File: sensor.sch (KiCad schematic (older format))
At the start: 53 parts, among them CON1 USB_B_Micro, U1 ESP-12F, U2 HTU21D, U3 PMS7003

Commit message: Use libraries from KiCad 4.0.7 instead of new from KiCad GitHub.
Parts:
- removed CON1: USB_B_Micro, Connectors_USB:USB_Micro-B_Molex-105017-0001, symbol USB_B_Micro
- added C?: 10uF/10V, Capacitor_SMD:C_0805_2012Metric, symbol C
- added C?: 100nF, Capacitor_SMD:C_0603_1608Metric, symbol C
- added CON1: Micro USB, Connectors_USB:USB_Micro-B_Molex-105017-0001, symbol USB_OTG
- added R? (x4): 10k, symbol R
- R13, R14, R15, R16: value 4k7 -> 10k
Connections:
- wire segments 153 -> 141
- no-connect marks 0 -> 8

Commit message: Working on connections
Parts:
- removed R25, R28, R33, R6: 130, symbol R
- removed R4: 180, symbol R
- added C?: 100nF, Capacitors_SMD:C_0603, symbol C
- added J?: Conn_01x05, symbol Conn_01x05
- added R35: 180, Resistors_SMD:R_0603, symbol R
- added R36, R37, R38, R39: 130, Resistors_SMD:R_0603, symbol R
- added R?: 10k, Resistors_SMD:R_0603, symbol R
- added SW?: RESET, symbol SW_Push
- added SW?: CFG, symbol SW_Push
- added TP1: PMS_SET, Wire_Pads:SolderWirePad_single_0-8mmDrill, symbol TEST_1P
- added TP2: PMS_RESET, Wire_Pads:SolderWirePad_single_0-8mmDrill, symbol TEST_1P
- added TP?: CFG, Wire_Pads:SolderWirePad_single_0-8mmDrill, symbol TEST_1P
- added TP?: RESET, Wire_Pads:SolderWirePad_single_0-8mmDrill, symbol TEST_1P
- C1: footprint Capacitor_SMD:C_0603_1608Metric -> Capacitors_SMD:C_0603
- C2: footprint Capacitor_SMD:C_0805_2012Metric -> Capacitors_SMD:C_0805
- C3: renamed from C?; footprint Capacitor_SMD:C_0805_2012Metric -> Capacitors_SMD:C_0805
- C4: renamed from C?; footprint Capacitor_SMD:C_0603_1608Metric -> Capacitors_SMD:C_0603
- Q1, Q2, Q3: renamed from Q?; footprint (none) -> TO_SOT_Packages_SMD:SOT-23
- R1, R10, R11, R12, R13, R14, R15, R16, R18, R2, R20, R21, R22, R24, R26, R3, R31, R32, R8: footprint (none) -> Resistors_SMD:R_0603
- R17, R23, R29, R30, R7: value 180 -> 130; footprint (none) -> Resistors_SMD:R_0603
- R19, R27, R34, R5, R9: value 130 -> 180; footprint (none) -> Resistors_SMD:R_0603
- R25, R28, R4, R6: renamed from R?; footprint (none) -> Resistors_SMD:R_0603
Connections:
- net +5V: now also J?.5 (Pin_5)
- net GND: now also C?.2, J?.4 (Pin_4), R?.2, SW?.2, SW?.2
- net LED_B: now also R17.2, R18.2, R23.2, R24.2, R31.2, R32.2, R8.2, R38.2, R39.2; no longer R12.2, R19.2, R22.2, R34.2, R9.2
- net LED_G: now also R12.2, R22.2, R29.2, R30.2, R7.2, R36.2, R37.2; no longer R18.2, R24.2, R27.2, R31.2, R32.2, R5.2, R8.2
- net LED_R: now also R19.2, R27.2, R34.2, R5.2, R9.2, R35.2; no longer R17.2, R23.2, R29.2, R30.2, R7.2
- net PMS_RESET: now also TP2.1
- net RESET: now reaches R6.2, U1.1 (RST)
- net RESET: now also C?.1, SW?.1, TP?.1
- net at U1.16 (GPIO15/BOOT2): now also R?.1
- net CFG_BTN: now reaches R28.2, U1.18 (GPIO0/BOOT0)
- net CFG_BTN: now also SW?.1, TP?.1
- net ESP_RXD: now reaches U1.21 (GPIO3/UART0_RXD)
- net ESP_RXD: now also J?.3 (Pin_3)
- net ESP_TXD: now reaches U1.22 (GPIO1/UART0_TXD)
- net ESP_TXD: now also J?.2 (Pin_2)
- net PMS_SET: now reaches R13.2, U3.10 (SET)
- net PMS_SET: now also TP1.1
- net at D2.4 (RK): now also R9.1
- net at D2.3 (GK): now also R11.1; no longer R5.1
- net at D2.2 (BK): now also R17.1
- net at D3.4 (RK): now also R19.1; no longer R7.1
- net at D3.3 (GK): now also R21.1; no longer R8.1
- net at D3.2 (BK): now also R23.1; no longer R9.1
- net at D7.4 (RK): now also R26.1; no longer R10.1
- net at D7.3 (GK): now also R29.1; no longer R11.1
- net at D7.2 (BK): now also R31.1; no longer R12.1
- net at D9.4 (RK): now also R34.1; no longer R29.1
- net at D9.3 (GK): now also R36.1; no longer R31.1
- net at D9.2 (BK): now also R38.1
- net at D4.2 (BK): now also R8.1; no longer R19.1
- net at D4.3 (GK): now also R7.1; no longer R18.1
- net at D4.4 (RK): now also R5.1; no longer R17.1
- net at D5.4 (RK): now also R10.1; no longer R20.1
- net at D5.3 (GK): now also R12.1; no longer R21.1
- net at D5.2 (BK): now also R18.1; no longer R22.1
- net at D6.4 (RK): now also R20.1; no longer R23.1
- net at R24.1: now also D6.2 (BK); no longer D6.3 (GK)
- net at D8.4 (RK): now also R27.1; no longer R26.1
- net at D8.3 (GK): now also R30.1; no longer R27.1
- net at D8.2 (BK): now also R32.1
- net at D10.4 (RK): now also R35.1; no longer R30.1
- net at D10.3 (GK): now also R37.1; no longer R32.1
- net at D10.2 (BK): now also R39.1; no longer R34.1
- net MCU_RXD renamed PMS_TXD
- net MCU_TXD renamed PMS_RXD
- net SCL renamed HTU_SCL
- net SDA renamed HTU_SDA
- new net: D6.3 (GK), R22.1
- no-connect marks 8 -> 9
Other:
- moved on the sheet: C1, C2, C3, C4, D1, D10, D2, D3, D4, D5, D6, D7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

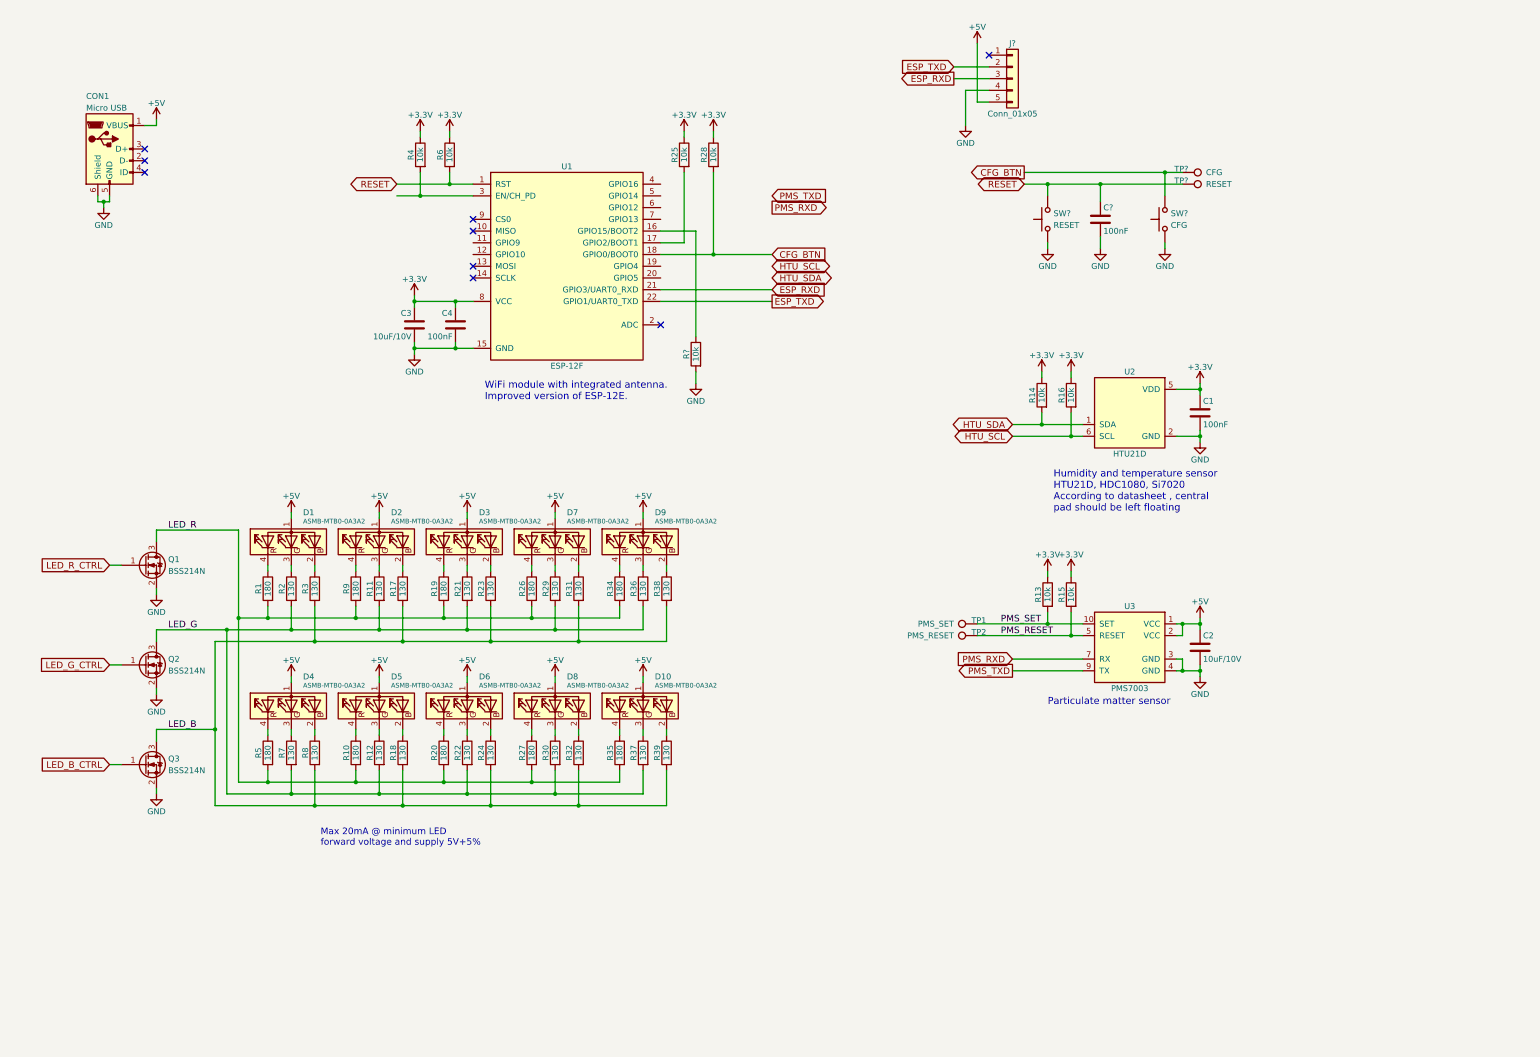
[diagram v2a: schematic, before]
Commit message: Add power supplies and other connections.
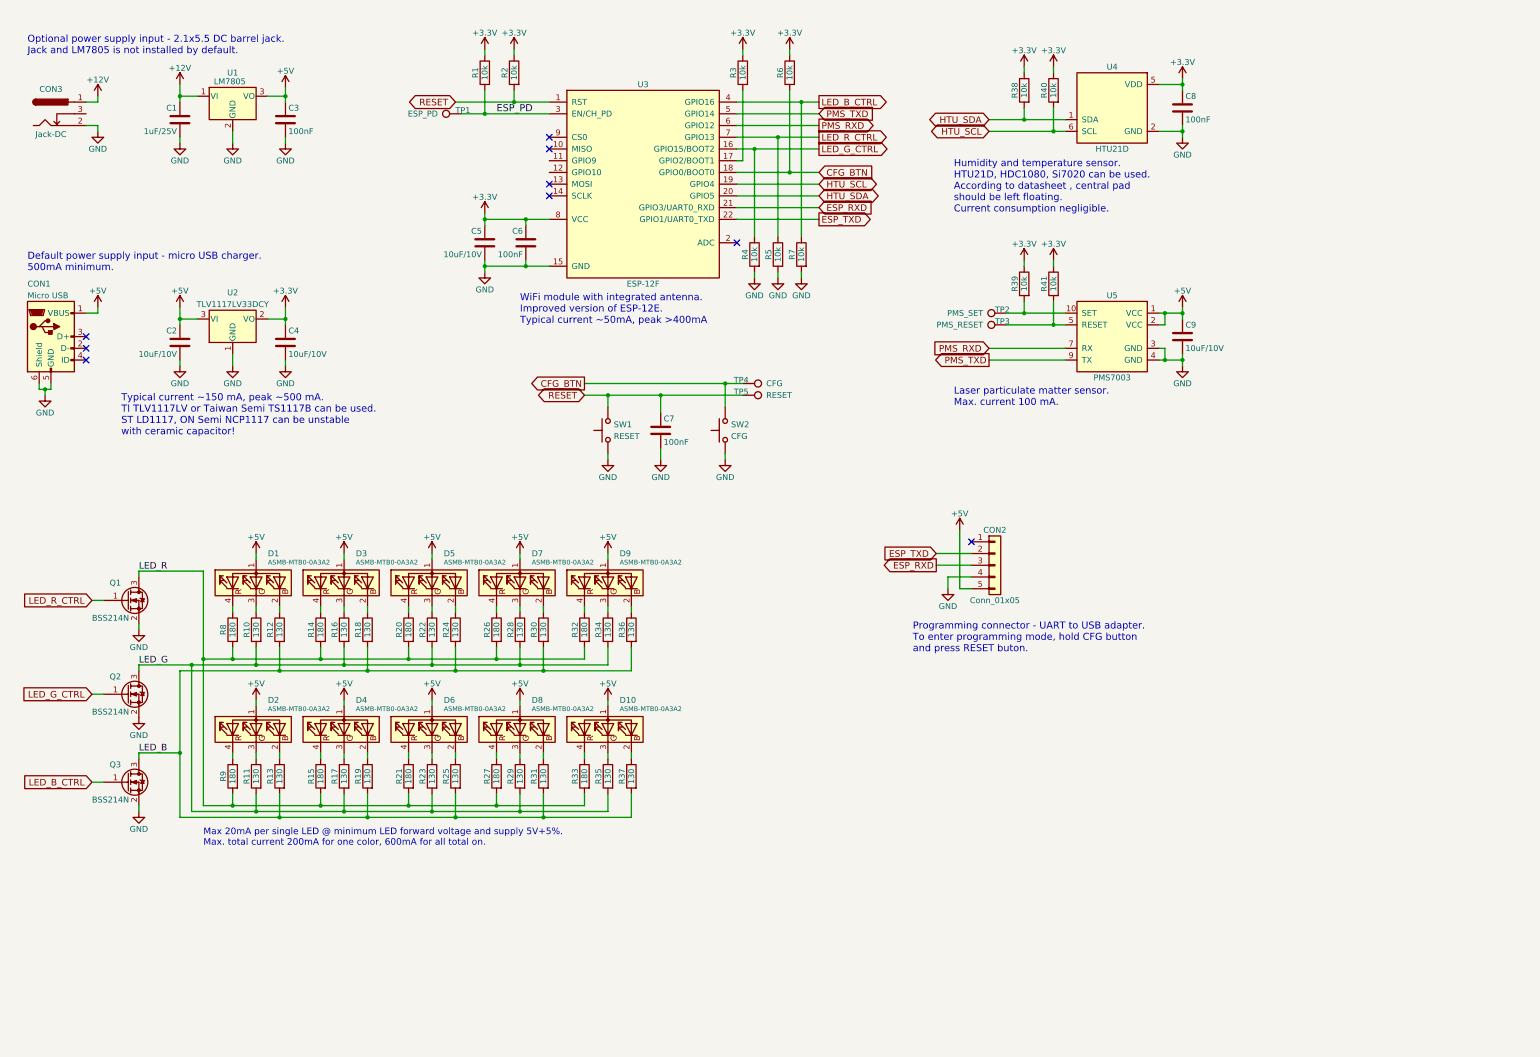
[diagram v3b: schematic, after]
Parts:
- added C1: 1uF/25V, Capacitors_SMD:C_0805, symbol C
- added C2, C4: 10uF/10V, Capacitors_SMD:C_0805, symbol C
- added C3: 100nF, Capacitors_SMD:C_0805, symbol C
- added CON3: Jack-DC, symbol Jack-DC
- added R5, R7: 10k, Resistors_SMD:R_1206, symbol R
- added TP1: ESP_PD, Wire_Pads:SolderWirePad_single_0-8mmDrill, symbol TEST_1P
- added U1: LM7805, TO_SOT_Packages_THT:TO-220_Horizontal, symbol LM7805_TO220
- added U2: TLV1117LV33DCY, TO_SOT_Packages_SMD:SOT-223-3Lead_TabPin2, symbol TLV1117-33
- C6: renamed from C4; footprint Capacitors_SMD:C_0603 -> Capacitors_SMD:C_0805
- C7: renamed from C?; footprint Capacitors_SMD:C_0603 -> Capacitors_SMD:C_0805
- C8: renamed from C1; footprint Capacitors_SMD:C_0603 -> Capacitors_SMD:C_0805
- CON2: renamed from J?; footprint (none) -> Pin_Headers:Pin_Header_Angled_1x05_Pitch2.54mm
- R1: renamed from R4; footprint Resistors_SMD:R_0603 -> Resistors_SMD:R_1206
- R10: renamed from R2; footprint Resistors_SMD:R_0603 -> Resistors_SMD:R_1206
- R11: renamed from R7; footprint Resistors_SMD:R_0603 -> Resistors_SMD:R_1206
- R12: renamed from R3; footprint Resistors_SMD:R_0603 -> Resistors_SMD:R_1206
- R13: renamed from R8; footprint Resistors_SMD:R_0603 -> Resistors_SMD:R_1206
- R14: renamed from R9; footprint Resistors_SMD:R_0603 -> Resistors_SMD:R_1206
- R15: renamed from R10; footprint Resistors_SMD:R_0603 -> Resistors_SMD:R_1206
- R16: renamed from R11; footprint Resistors_SMD:R_0603 -> Resistors_SMD:R_1206
- R17: renamed from R12; footprint Resistors_SMD:R_0603 -> Resistors_SMD:R_1206
- R18: renamed from R17; footprint Resistors_SMD:R_0603 -> Resistors_SMD:R_1206
- R19: renamed from R18; footprint Resistors_SMD:R_0603 -> Resistors_SMD:R_1206
- R2: renamed from R6; footprint Resistors_SMD:R_0603 -> Resistors_SMD:R_1206
- R20: renamed from R19; footprint Resistors_SMD:R_0603 -> Resistors_SMD:R_1206
- R21: renamed from R20; footprint Resistors_SMD:R_0603 -> Resistors_SMD:R_1206
- R22: renamed from R21; footprint Resistors_SMD:R_0603 -> Resistors_SMD:R_1206
- R23: renamed from R22; footprint Resistors_SMD:R_0603 -> Resistors_SMD:R_1206
- R24: renamed from R23; footprint Resistors_SMD:R_0603 -> Resistors_SMD:R_1206
- R25: renamed from R24; footprint Resistors_SMD:R_0603 -> Resistors_SMD:R_1206
- R26, R27: footprint Resistors_SMD:R_0603 -> Resistors_SMD:R_1206
- R28: renamed from R29; footprint Resistors_SMD:R_0603 -> Resistors_SMD:R_1206
- R29: renamed from R30; footprint Resistors_SMD:R_0603 -> Resistors_SMD:R_1206
- R3: renamed from R25; footprint Resistors_SMD:R_0603 -> Resistors_SMD:R_1206
- R30: renamed from R31; footprint Resistors_SMD:R_0603 -> Resistors_SMD:R_1206
- R31: renamed from R32; footprint Resistors_SMD:R_0603 -> Resistors_SMD:R_1206
- R32: renamed from R34; footprint Resistors_SMD:R_0603 -> Resistors_SMD:R_1206
- R33: renamed from R35; footprint Resistors_SMD:R_0603 -> Resistors_SMD:R_1206
- R34: renamed from R36; footprint Resistors_SMD:R_0603 -> Resistors_SMD:R_1206
- R35: renamed from R37; footprint Resistors_SMD:R_0603 -> Resistors_SMD:R_1206
- R36: renamed from R38; footprint Resistors_SMD:R_0603 -> Resistors_SMD:R_1206
- R37: renamed from R39; footprint Resistors_SMD:R_0603 -> Resistors_SMD:R_1206
- R38: renamed from R14; footprint Resistors_SMD:R_0603 -> Resistors_SMD:R_1206
- R39: renamed from R13; footprint Resistors_SMD:R_0603 -> Resistors_SMD:R_1206
- R4: renamed from R?; footprint Resistors_SMD:R_0603 -> Resistors_SMD:R_1206
- R40: renamed from R16; footprint Resistors_SMD:R_0603 -> Resistors_SMD:R_1206
- R41: renamed from R15; footprint Resistors_SMD:R_0603 -> Resistors_SMD:R_1206
- R6: renamed from R28; footprint Resistors_SMD:R_0603 -> Resistors_SMD:R_1206
- R8: renamed from R1; footprint Resistors_SMD:R_0603 -> Resistors_SMD:R_1206
- R9: renamed from R5; footprint Resistors_SMD:R_0603 -> Resistors_SMD:R_1206
- gave numbers to parts that had none: 4
- renumbered C3 to C5, C2 to C9, D4 to D2, D2 to D3, D5 to D4, D3 to D5, TP1 to TP2, TP2 to TP3, U1 to U3, U2 to U4, U3 to U5
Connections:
- net +3V3: now also C4.1, U2.2 (VO)
- net +5V: now also C2.1, C3.1, U1.3 (VO), U2.3 (VI)
- net GND: now also C1.2, C2.2, C3.2, C4.2, CON3.2, R5.2, R7.2, U1.2 (GND), U2.1 (GND)
- net HTU_SCL: now also U3.19 (GPIO4)
- net HTU_SDA: now also U3.20 (GPIO5)
- net LED_B_CTRL: now also U3.4 (GPIO16), R7.1
- net LED_G_CTRL: now also R4.1, U3.16 (GPIO15/BOOT2)
- net LED_R_CTRL: now also U3.7 (GPIO13), R5.1
- net PMS_RXD: now also U3.6 (GPIO12)
- net PMS_TXD: now also U3.5 (GPIO14)
- net ESP_PD: now reaches R1.2, U3.3 (EN/CH_PD)
- net ESP_PD: now also TP1.1
- net PMS_RESET: no longer names the net of R41.2, TP3.1, U5.5 (RESET)
- net PMS_SET: no longer names the net of R39.2, TP2.1, U5.10 (SET)
- new net +12V: C1.1, CON3.1, U1.1 (VI)
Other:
- note added: "Default power supply input - micro USB charger.\n500mA minimum."
- note added: "Humidity and temperature sensor.\nHTU21D, HDC1080, Si7020 can be used.\nAccording to datasheet , central pad \nshould be left floating.\nCurrent consumption negligible."
- note added: "Laser particulate matter sensor.\nMax. current 100 mA."
- note added: "Max 20mA per single LED @ minimum LED forward voltage and supply 5V+5%.\nMax. total current 200mA for one color, 600mA for all total on."
- note added: "Optional power supply input - 2.1x5.5 DC barrel jack.\nJack and LM7805 is not installed by default."
- note added: "Programming connector - UART to USB adapter.\nTo enter programming mode, hold CFG button\nand press RESET buton."
- note added: "Typical current ~~150 mA, peak ~~500 mA.\nTI TLV1117LV or Taiwan Semi TS1117B can be used.\nST LD1117, ON Semi NCP1117 can be unstable \nwith ceramic capacitor!"
- note added: "WiFi module with integrated antenna.\nImproved version of ESP-12E.\nTypical current ~~50mA, peak >400mA"
- note removed: "Humidity and temperature sensor\nHTU21D, HDC1080, Si7020\nAccording to datasheet , central \npad should be left floating"
- note removed: "Max 20mA @ minimum LED\nforward voltage and supply 5V+5%"
- note removed: "Particulate matter sensor"
- note removed: "WiFi module with integrated antenna.\nImproved version of ESP-12E."
- moved on the sheet: C5, C6, C7, C8, C9, CON1, CON2, D1, D10, D2, D3, D4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

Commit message: Change packages to bigger ones, simpler to assemble.
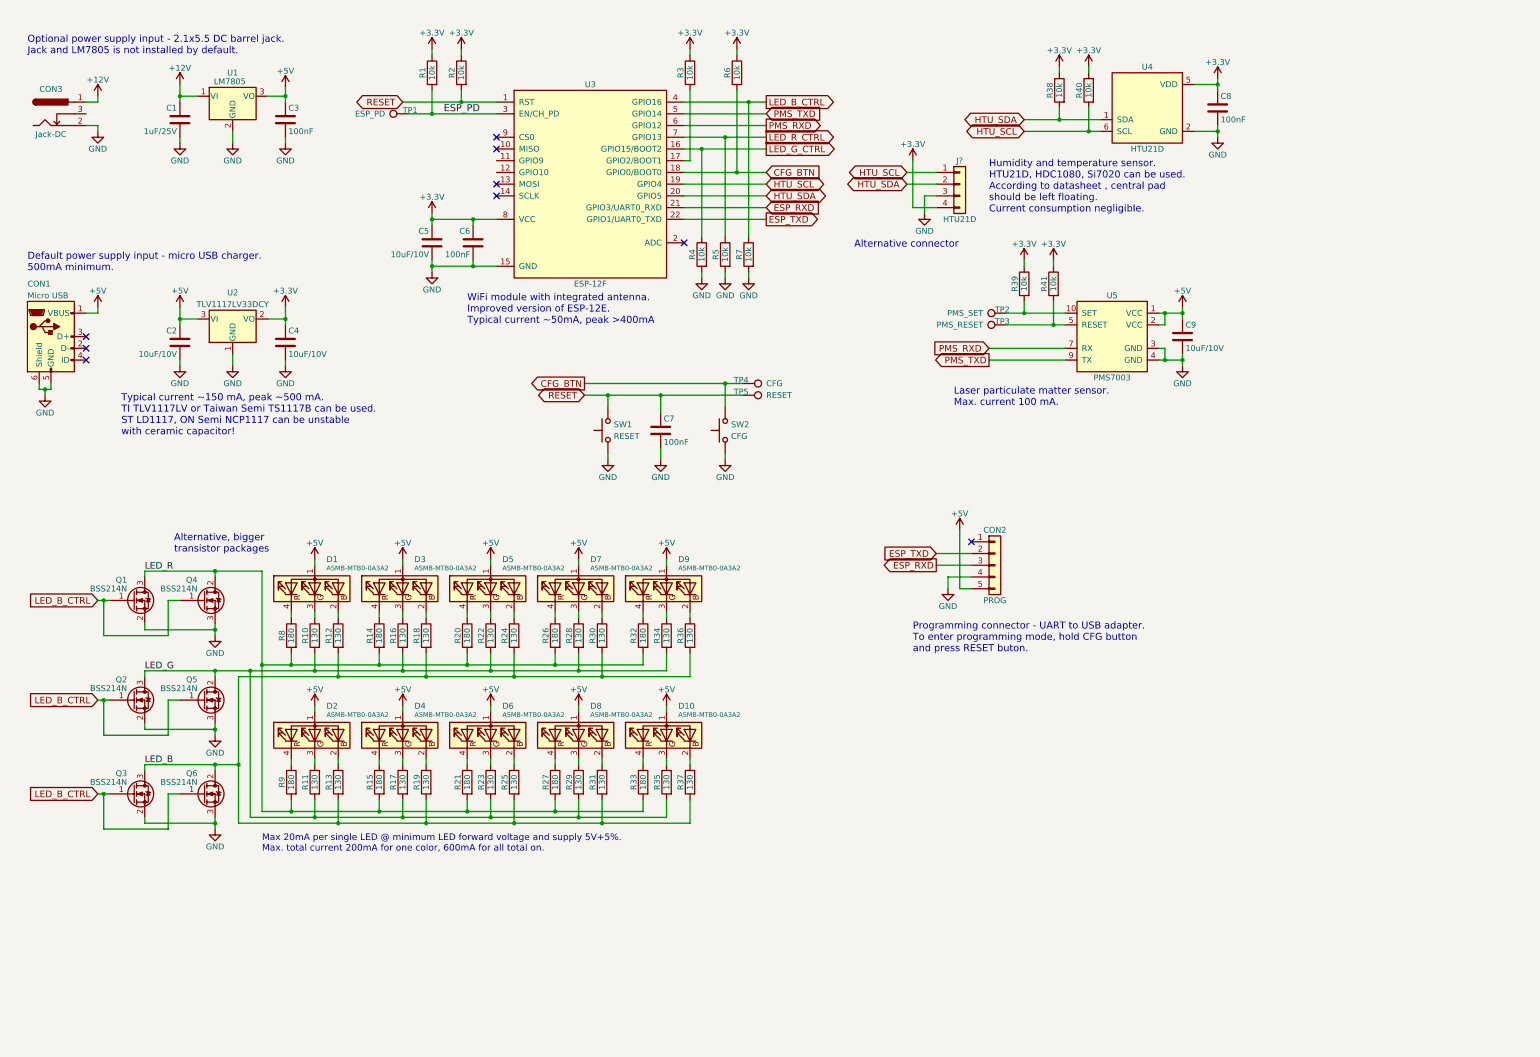
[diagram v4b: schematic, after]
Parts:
- added J?: HTU21D, symbol Conn_01x04
- added Q4, Q5, Q6: BSS214N, TO_SOT_Packages_SMD:SOT-223-3Lead_TabPin2, symbol Q_NMOS_GDS
- CON2: value Conn_01x05 -> PROG
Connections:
- net +3V3: now also J?.4 (Pin_4)
- net GND: now also J?.3 (Pin_3), Q4.3 (S), Q5.3 (S), Q6.3 (S)
- net HTU_SCL: now also J?.1 (Pin_1)
- net HTU_SDA: now also J?.2 (Pin_2)
- net LED_B: now also Q6.2 (D)
- net LED_B_CTRL: now also Q1.1 (G), Q2.1 (G), Q4.1 (G), Q5.1 (G), Q6.1 (G)
- net LED_G: now also Q5.2 (D)
- net LED_G_CTRL: no longer Q2.1 (G)
- net LED_R: now also Q4.2 (D)
- net LED_R_CTRL: no longer Q1.1 (G)
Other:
- note added: "Alternative connector"
- note added: "Alternative, bigger\ntransistor packages"
- moved on the sheet: C5, C6, C8, D1, D10, D2, D3, D4, D5, D6, D7, D8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
